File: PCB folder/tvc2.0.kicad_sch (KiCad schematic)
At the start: 11 parts, among them J1 Servo2, J2 Servo1, J3 PWM Test OUT, U1 Teensy4.1, U5 LM7805_TO220

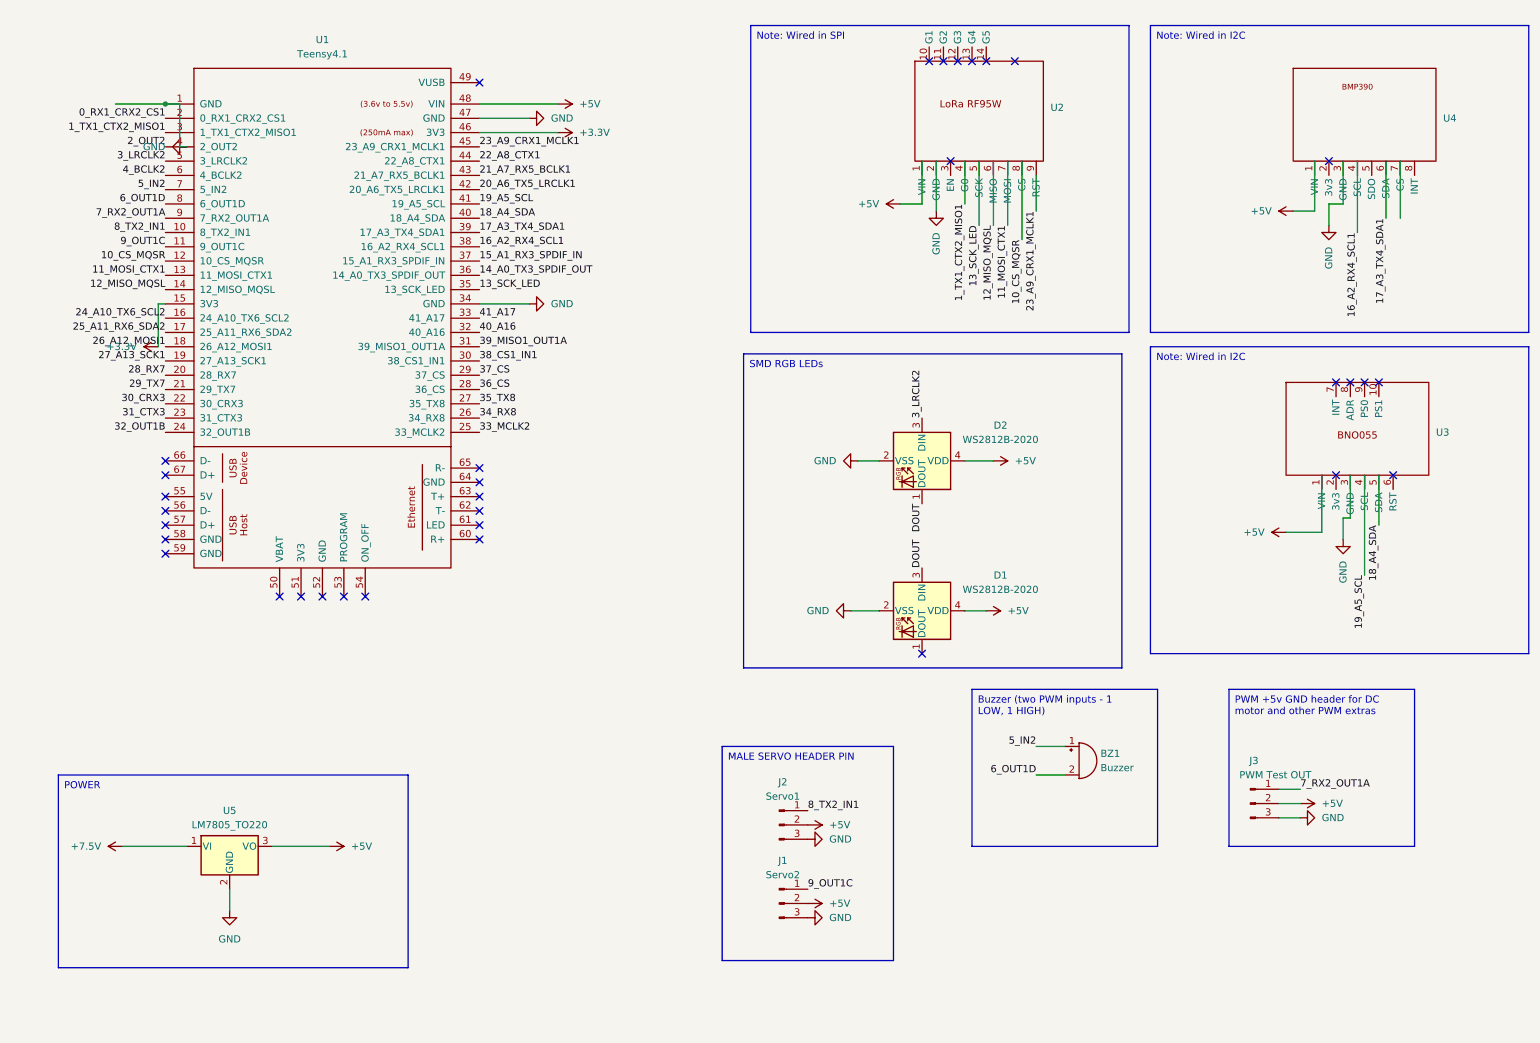
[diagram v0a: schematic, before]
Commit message: funts: Added Pyro circuit in schematic
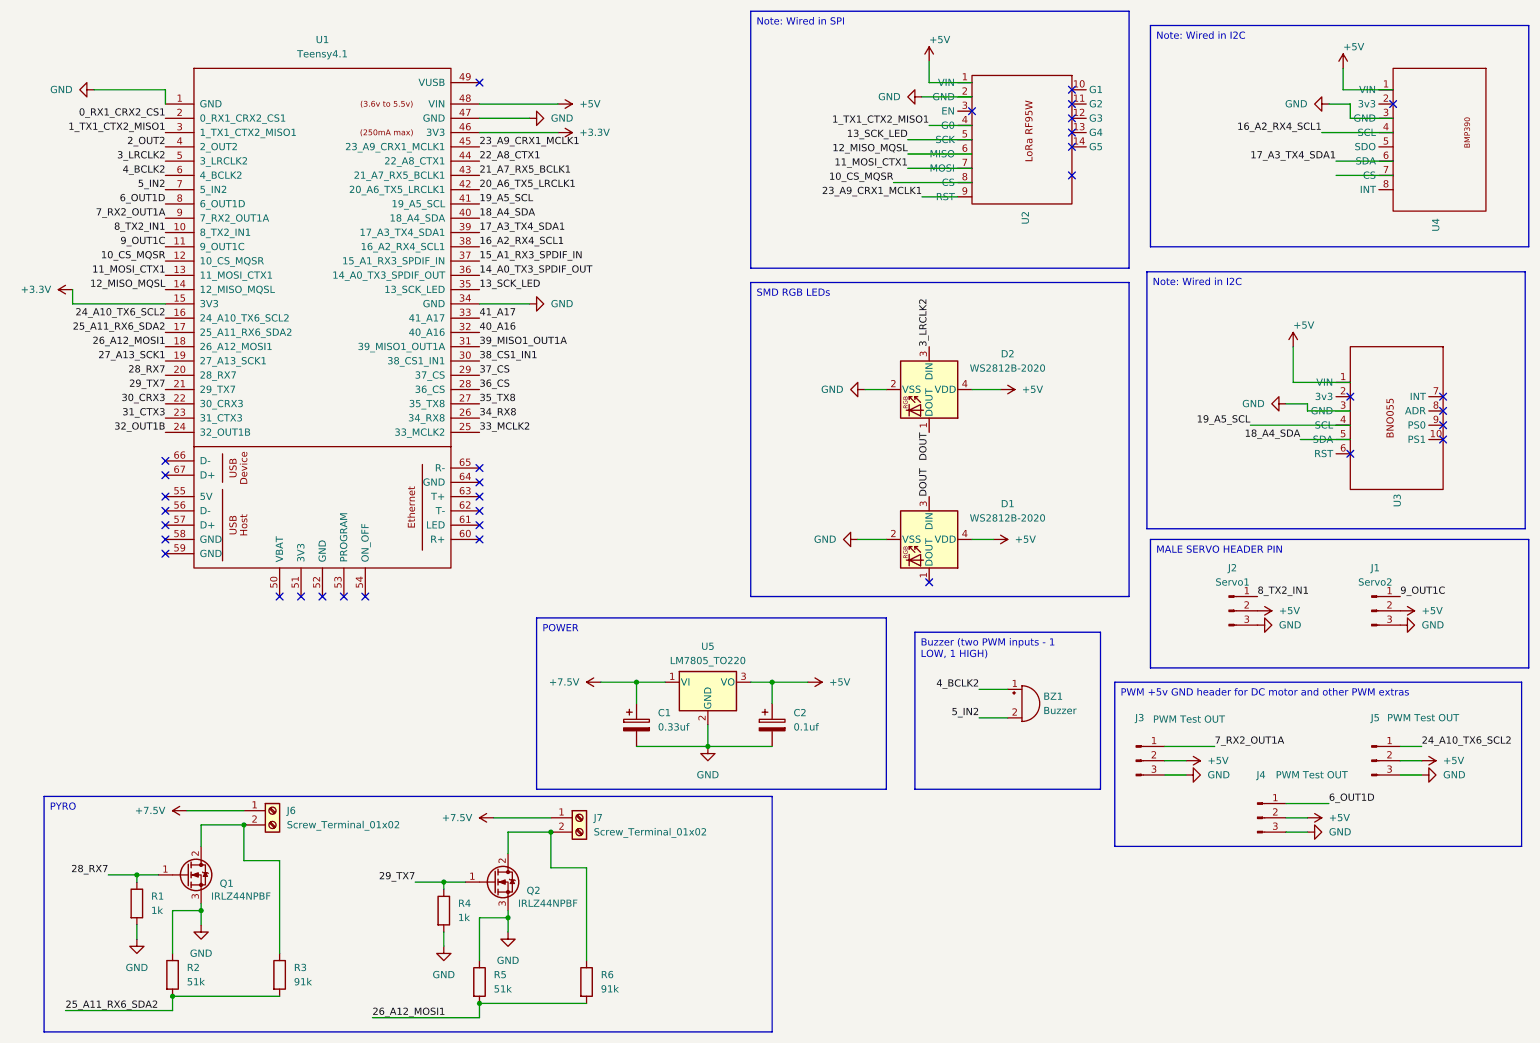
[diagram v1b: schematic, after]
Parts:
- added C1: 0.33uf, symbol Device:C_Polarized
- added C2: 0.1uf, symbol Device:C_Polarized
- added J4, J5: PWM Test OUT, Connector_PinHeader_2.54mm:PinHeader_1x03_P2.54mm_Vertical, symbol Connector:Conn_01x03_Pin
- added J6, J7: Screw_Terminal_01x02, symbol Connector:Screw_Terminal_01x02
- added Q1, Q2: IRLZ44NPBF, Package_TO_SOT_THT:TO-220-3_Vertical, symbol Transistor_FET:IRLZ44N
- added R1, R4: 1k, symbol Device:R
- added R2, R5: 51k, symbol Device:R
- added R3, R6: 91k, symbol Device:R
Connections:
- net +5V: now also C2.1, J4.2 (Pin_2), J5.2 (Pin_2)
- net +7.5V: now also C1.1, J6.1 (Pin_1), J7.1 (Pin_1)
- net 24_A10_TX6_SCL2: now also J5.1 (Pin_1)
- net 25_A11_RX6_SDA2: now also R2.2, R3.2
- net 26_A12_MOSI1: now also R5.2, R6.2
- net 28_RX7: now also Q1.1 (G), R1.1
- net 29_TX7: now also Q2.1 (G), R4.1
- net 4_BCLK2: now also BZ1.1 (+)
- net 5_IN2: now also BZ1.2 (-); no longer BZ1.1 (+)
- net 6_OUT1D: now also J4.1 (Pin_1); no longer BZ1.2 (-)
- net GND: now also C1.2, C2.2, J4.3 (Pin_3), J5.3 (Pin_3), Q1.3 (S), Q2.3 (S), R1.2, R2.1, R4.2, R5.1
- new net: J7.2 (Pin_2), Q2.2 (D), R6.1
- new net: J6.2 (Pin_2), Q1.2 (D), R3.1
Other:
- moved on the sheet: BZ1, D1, D2, J1, J2, J3, U2, U3, U4, U5

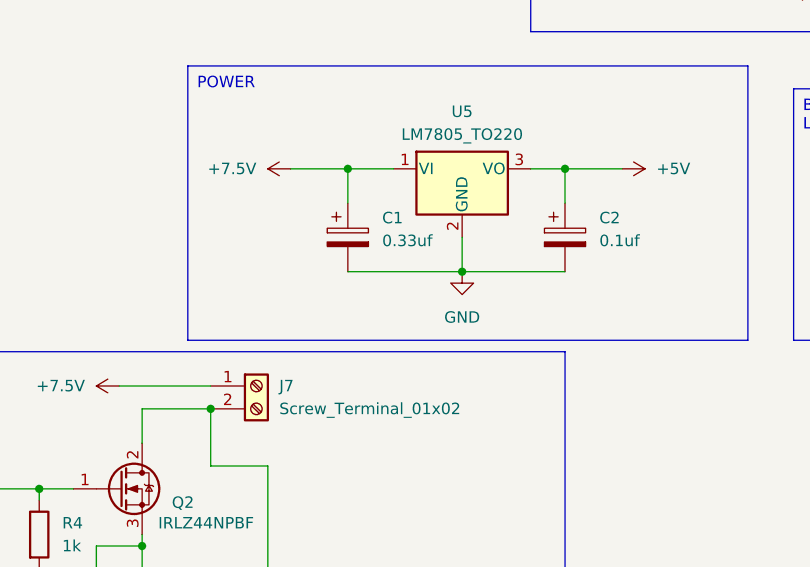
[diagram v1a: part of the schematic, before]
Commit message: functs: update PCB, add part excel
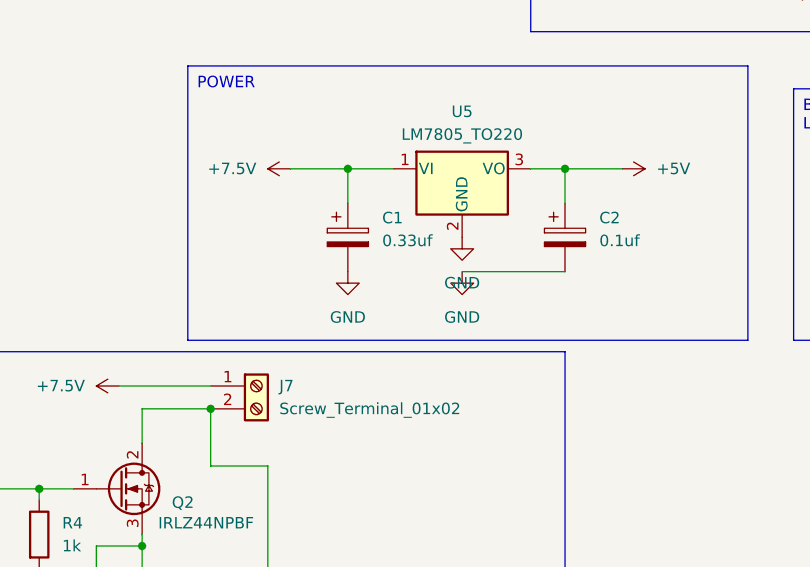
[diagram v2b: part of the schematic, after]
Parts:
- C1, C2: footprint (none) -> Capacitor_SMD:C_1206_3216Metric
- J6, J7: footprint (none) -> TerminalBlock_Phoenix:TerminalBlock_Phoenix_MKDS-1,5-2-5.08_1x02_P5.08mm_Horizontal
- R1, R2, R3, R4, R5, R6: footprint (none) -> Resistor_SMD:R_1206_3216Metric
- U1: footprint Teensy4.1:Teensy41 -> tvc499:Teensy41
- U2: footprint LoRa_RF95:LoRa_RF95 Breakout -> tvc499:LoRa_RF95 Breakout
- U3: footprint BNO055:BNO055 -> tvc499:BNO055
- U5: footprint Package_TO_SOT_THT:TO-220-3_Vertical -> Package_TO_SOT_SMD:SOT-223
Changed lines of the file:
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@@
 	)
 	(junction
-		(at 137.16 144.78)
-		(diameter 0)
-		(color 0 0 0 0)
-	)
-	(junction
 		(at 46.99 173.99)
 		(diameter 0)
@@
 	(wire
 		(pts
-			(xy 137.16 140.97) (xy 137.16 144.78)
-		)
-		(stroke
-			(width 0)
-			(type default)
-		)
-	)
-	(wire
-		(pts
 			(xy 35.56 167.64) (xy 39.37 167.64)
 		)
@@
 	(wire
 		(pts
-			(xy 124.46 144.78) (xy 137.16 144.78)
-		)
-		(stroke
-			(width 0)
-			(type default)
-		)
-	)
-	(wire
-		(pts
 			(xy 90.17 168.91) (xy 90.17 170.18)
 		)
@@
 			)
 		)
-		(property "Footprint" ""
+		(property "Footprint" "TerminalBlock_Phoenix:TerminalBlock_Phoenix_MKDS-1,5-2-5.08_1x02_P5.08mm_Horizontal"
 			(at 114.3 157.48 0)
 			(effects
@@
 			)
 		)
-		(property "Footprint" ""
+		(property "Footprint" "Resistor_SMD:R_1206_3216Metric"
 			(at 88.392 173.99 90)
 			(effects
@@
 			)
 		)
-		(property "Footprint" "Package_TO_SOT_THT:TO-220-3_Vertical"
+		(property "Footprint" "Package_TO_SOT_SMD:SOT-223"
 			(at 137.16 127.635 0)
 			(effects
@@
 			)
 		)
-		(property "Footprint" "BNO055:BNO055"
+		(property "Footprint" "tvc499:BNO055"
 			(at 259.08 86.36 0)
 			(effects
@@
 			)
 		)
-		(property "Footprint" ""
+		(property "Footprint" "Capacitor_SMD:C_1206_3216Metric"
 			(at 149.5552 144.78 0)
 			(effects
@@
 			)
 		)
-		(property "Footprint" ""
+		(property "Footprint" "Resistor_SMD:R_1206_3216Metric"
 			(at 94.742 186.69 90)
 			(effects
@@
 	)
 	(symbol
+		(lib_id "power:GND")
+		(at 124.46 144.78 0)
+		(unit 1)
+		(exclude_from_sim no)
+		(in_bom yes)
+		(on_board yes)
+		(dnp no)
+		(fields_autoplaced yes)
+		(property "Reference" "#PWR036"
+			(at 124.46 151.13 0)
+			(effects
+				(font
+					(size 1.27 1.27)
+				)
+				(hide yes)
+			)
+		)
+		(property "Value" "GND"
+			(at 124.46 149.86 0)
+			(effects
+				(font
+					(size 1.27 1.27)
+				)
+			)
+		)
+		(property "Footprint" ""
+			(at 124.46 144.78 0)
+			(effects
+				(font
+					(size 1.27 1.27)
+				)
+				(hide yes)
+			)
+		)
+		(property "Datasheet" ""
+			(at 124.46 144.78 0)
+			(effects
+				(font
+					(size 1.27 1.27)
+				)
+				(hide yes)
+			)
+		)
+		(property "Description" "Power symbol creates a global label with name \"GND\" , ground"
+			(at 124.46 144.78 0)
+			(effects
+				(font
+					(size 1.27 1.27)
+				)
+				(hide yes)
+			)
+		)
+		(pin "1"
+		)
+		(instances
+			(project "tvc2.0"
+				(path "/3cebab3b-ef7a-41c0-87f0-9665bea660f9"
+					(reference "#PWR036")
+					(unit 1)
+				)
+			)
+		)
+	)
+	(symbol
 		(lib_id "Connector:Conn_01x03_Pin")
 		(at 255.27 120.65 0)
@@
 			)
 		)
-		(property "Footprint" ""
+		(property "Footprint" "Resistor_SMD:R_1206_3216Metric"
 			(at 113.792 186.69 90)
 			(effects
@@
 			)
 		)
-		(property "Footprint" ""
+		(property "Footprint" "Resistor_SMD:R_1206_3216Metric"
 			(at 59.182 185.42 90)
 			(effects
@@
 			)
 		)
-		(property "Footprint" "Teensy4.1:Teensy41"
+		(property "Footprint" "tvc499:Teensy41"
 			(at 58.42 74.93 0)
 			(effects
@@
 			)
 		)
-		(property "Footprint" ""
+		(property "Footprint" "Resistor_SMD:R_1206_3216Metric"
 			(at 33.782 172.72 90)
 			(effects
@@
 			)
 		)
-		(property "Footprint" "LoRa_RF95:LoRa_RF95 Breakout"
+		(property "Footprint" "tvc499:LoRa_RF95 Breakout"
 			(at 194.31 34.29 0)
 			(effects
@@
 	)
 	(symbol
+		(lib_id "power:GND")
+		(at 137.16 140.97 0)
+		(unit 1)
+		(exclude_from_sim no)
+		(in_bom yes)
+		(on_board yes)
+		(dnp no)
+		(fields_autoplaced yes)
+		(property "Reference" "#PWR037"
+			(at 137.16 147.32 0)
+			(effects
+				(font
+					(size 1.27 1.27)
+				)
+				(hide yes)
+			)
+		)
+		(property "Value" "GND"
+			(at 137.16 146.05 0)
+			(effects
+				(font
+					(size 1.27 1.27)
+				)
+			)
+		)
+		(property "Footprint" ""
+			(at 137.16 140.97 0)
+			(effects
+				(font
+					(size 1.27 1.27)
+				)
+				(hide yes)
+			)
+		)
+		(property "Datasheet" ""
+			(at 137.16 140.97 0)
+			(effects
+				(font
+					(size 1.27 1.27)
+				)
+				(hide yes)
+			)
+		)
+		(property "Description" "Power symbol creates a global label with name \"GND\" , ground"
+			(at 137.16 140.97 0)
+			(effects
+				(font
+					(size 1.27 1.27)
+				)
+				(hide yes)
+			)
+		)
+		(pin "1"
+		)
+		(instances
+			(project "tvc2.0"
+				(path "/3cebab3b-ef7a-41c0-87f0-9665bea660f9"
+					(reference "#PWR037")
+					(unit 1)
+				)
+			)
+		)
+	)
+	(symbol
 		(lib_id "power:+5V")
 		(at 222.25 147.32 270)
@@
 			)
 		)
-		(property "Footprint" ""
+		(property "Footprint" "TerminalBlock_Phoenix:TerminalBlock_Phoenix_MKDS-1,5-2-5.08_1x02_P5.08mm_Horizontal"
 			(at 59.69 156.21 0)
 			(effects
@@
 			)
 		)
-		(property "Footprint" ""
+		(property "Footprint" "Resistor_SMD:R_1206_3216Metric"
 			(at 40.132 185.42 90)
 			(effects
@@
 			)
 		)
-		(property "Footprint" ""
+		(property "Footprint" "Capacitor_SMD:C_1206_3216Metric"
 			(at 125.4252 144.78 0)
 			(effects

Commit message: edit: final pcb files sent to JLC
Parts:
- U4: footprint (none) -> tvc499:BMP390
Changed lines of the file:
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@@
 			)
 		)
-		(property "Footprint" ""
+		(property "Footprint" "tvc499:BMP390"
 			(at 265.43 35.56 0)
 			(effects
